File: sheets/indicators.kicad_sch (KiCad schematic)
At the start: 18 parts, among them Q1 AO3400A

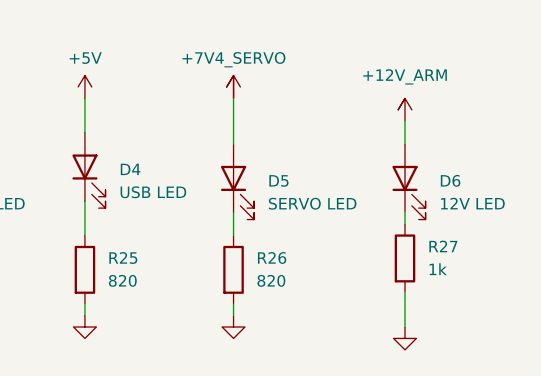
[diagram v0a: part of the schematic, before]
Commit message: Cleared ALL ERC warnings
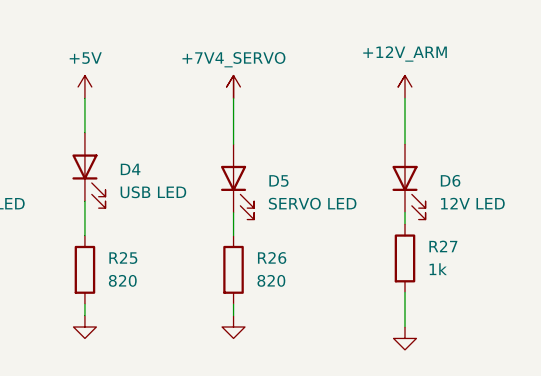
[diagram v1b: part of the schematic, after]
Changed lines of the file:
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@@
 	(wire
 		(pts
-			(xy 213.36 29.21) (xy 213.36 31.75)
+			(xy 213.36 26.67) (xy 213.36 31.75)
 		)
 		(stroke
@@
 	(symbol
 		(lib_id "aerolotl_custom:+12V_ARM")
-		(at 213.36 29.21 0)
+		(at 213.36 26.67 0)
 		(unit 1)
 		(exclude_from_sim no)
@@
 		(fields_autoplaced yes)
 		(property "Reference" "#PWR078"
-			(at 213.36 29.21 0)
+			(at 213.36 26.67 0)
 			(effects
 				(font
@@
 		)
 		(property "Value" "+12V_ARM"
-			(at 213.36 24.13 0)
-			(effects
-				(font
-					(size 1.27 1.27)
-				)
-			)
-		)
-		(property "Footprint" ""
-			(at 213.36 29.21 0)
+			(at 213.36 21.59 0)
+			(effects
+				(font
+					(size 1.27 1.27)
+				)
+			)
+		)
+		(property "Footprint" ""
+			(at 213.36 26.67 0)
 			(effects
 				(font
@@
 		)
 		(property "Datasheet" ""
-			(at 213.36 29.21 0)
+			(at 213.36 26.67 0)
 			(effects
 				(font
@@
 		)
 		(property "Description" ""
-			(at 213.36 29.21 0)
-			(effects
-				(font
+			(at 213.36 26.67 0)
+			(effects
+				(font

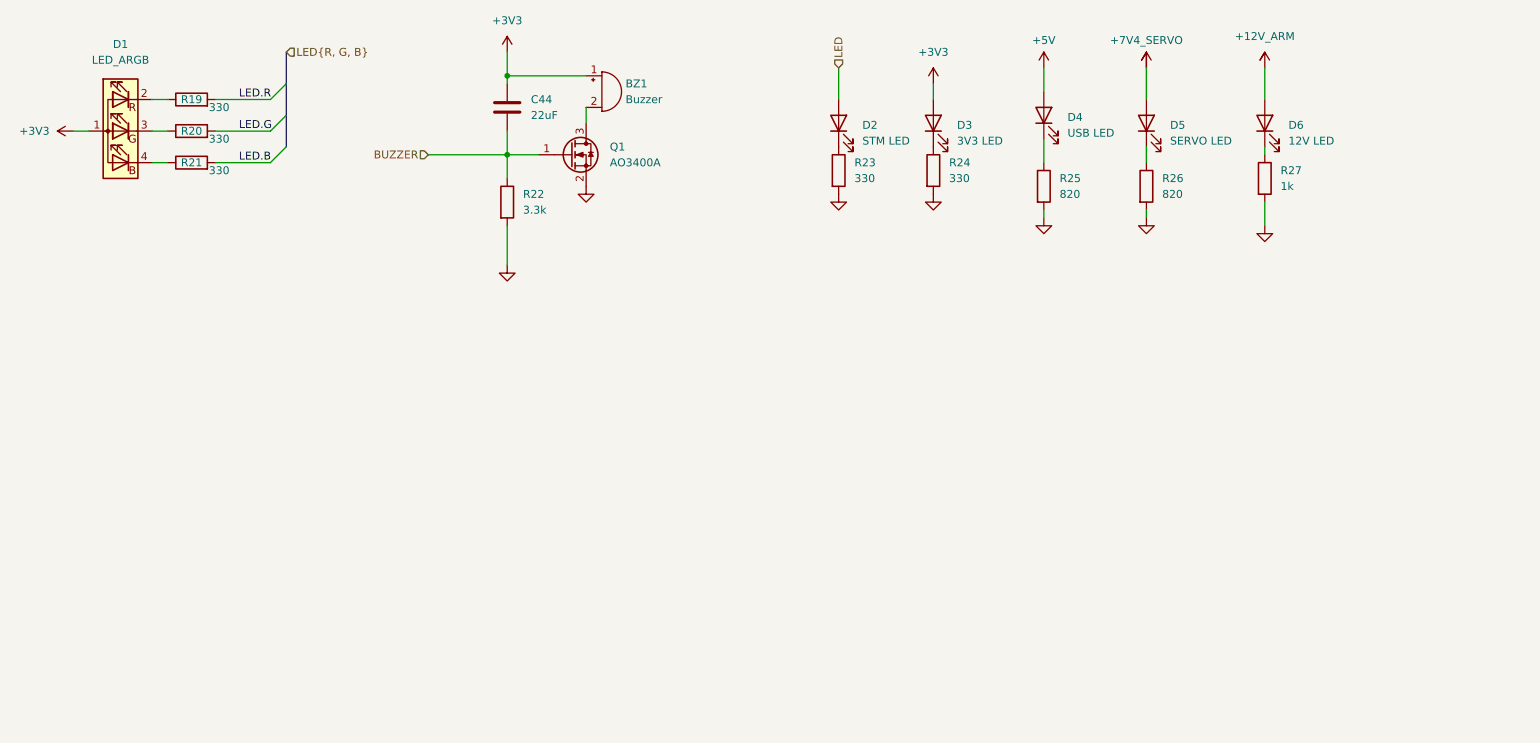
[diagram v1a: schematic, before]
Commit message: letter size schematic pages formatted
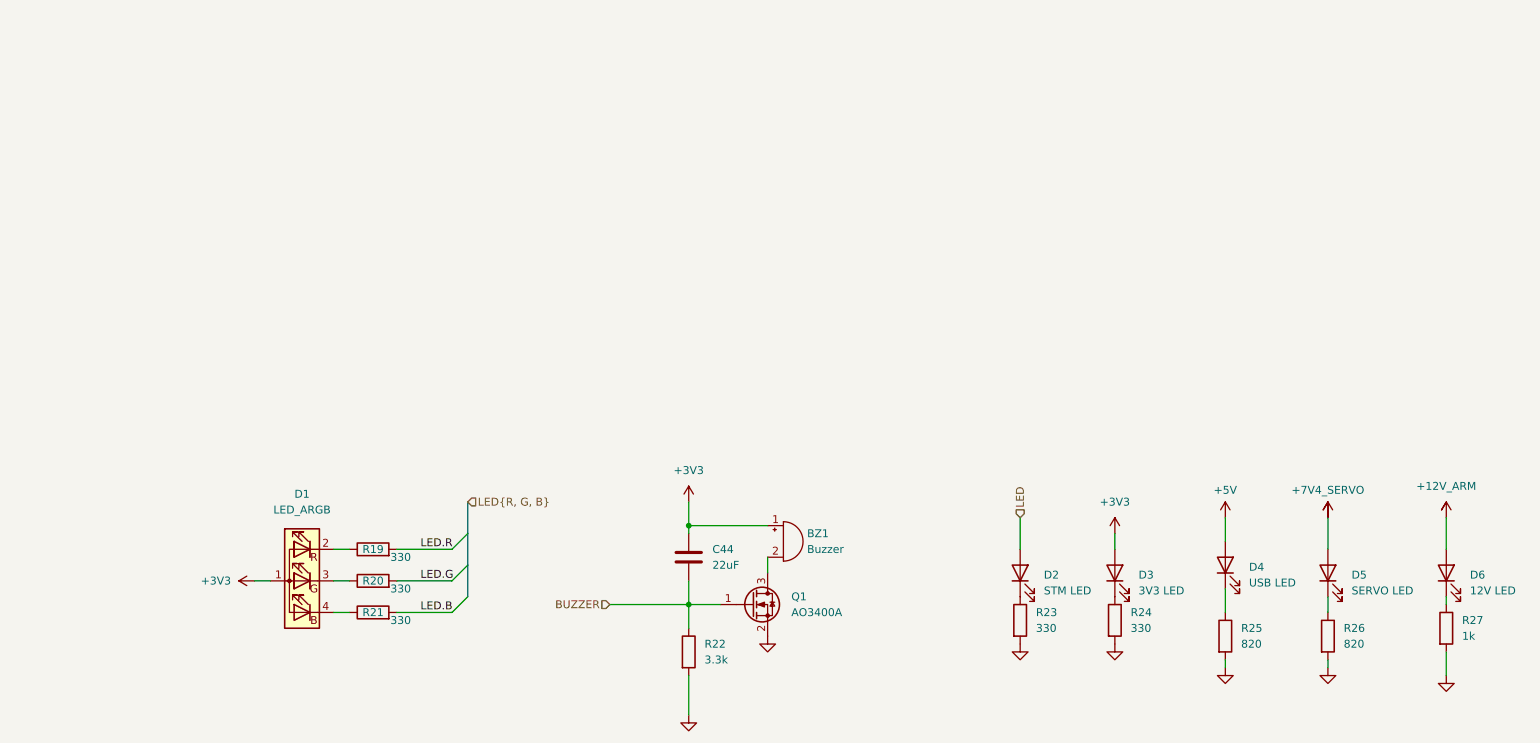
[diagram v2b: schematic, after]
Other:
- company: (none) -> Stanford Space Initiative
- title: (none) -> AEROLOTL NEW COLLINS FLIGHT COMPUTER
- moved on the sheet: BZ1, C44, D2, D3, D4, D5, D6, Q1, R19, R20, R21, R22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
